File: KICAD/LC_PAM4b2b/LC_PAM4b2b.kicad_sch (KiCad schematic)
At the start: 18 parts, among them J1 Conn_01x02_Male, J10 Micro_SD_Board, J2 Conn_01x02_Male, J3 Conn_01x03_Pin, J4 Conn_01x02_Pin, J6 RTC, J7 Conn_01x03_Pin

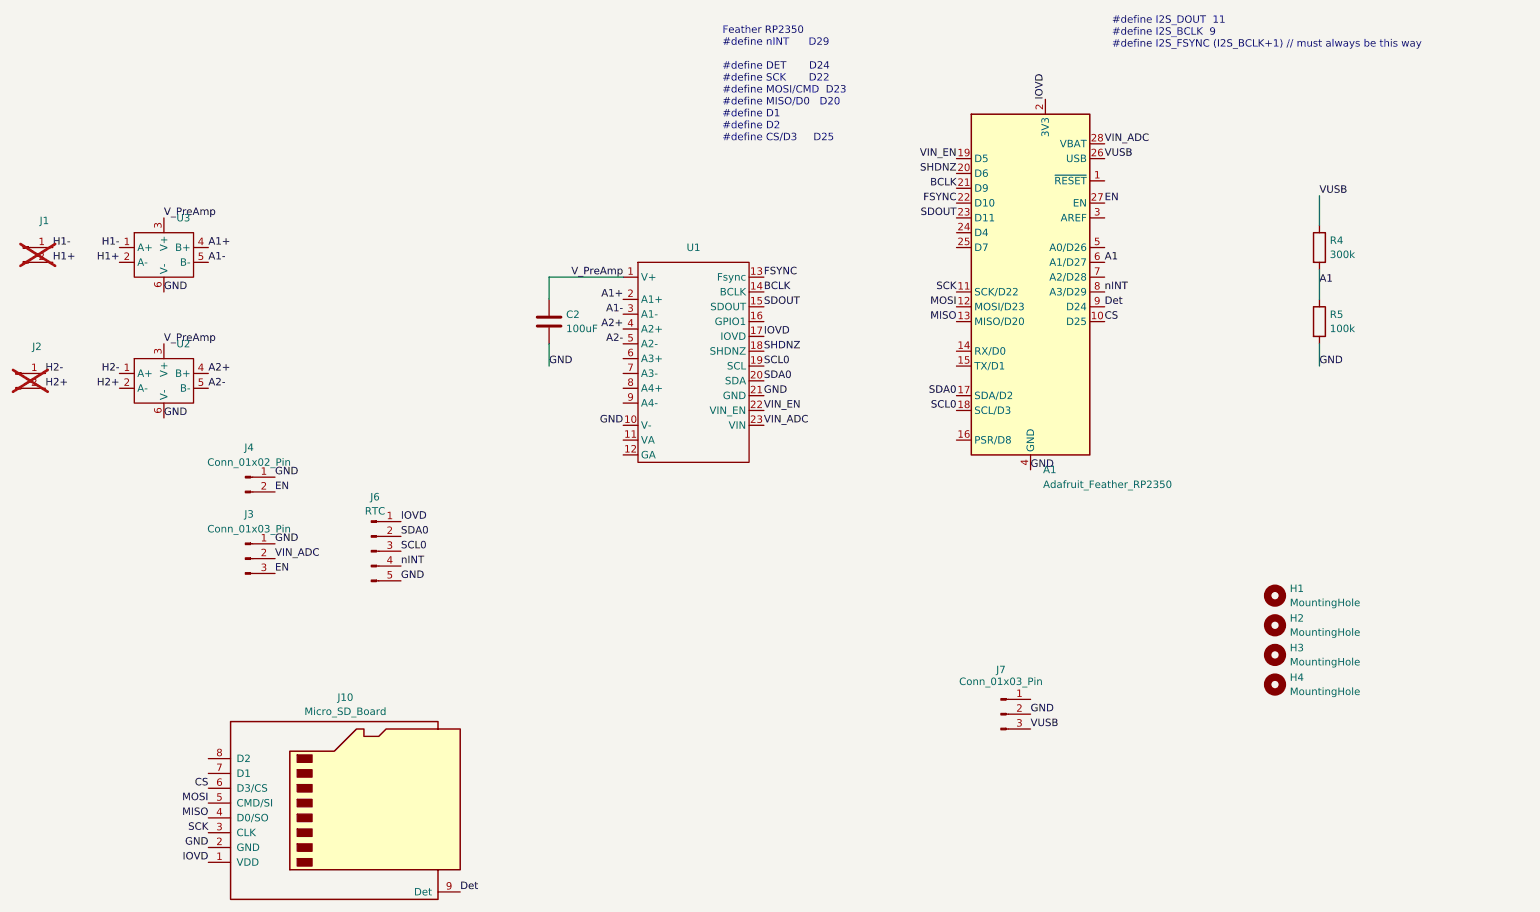
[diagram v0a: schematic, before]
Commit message: corrected hibernate
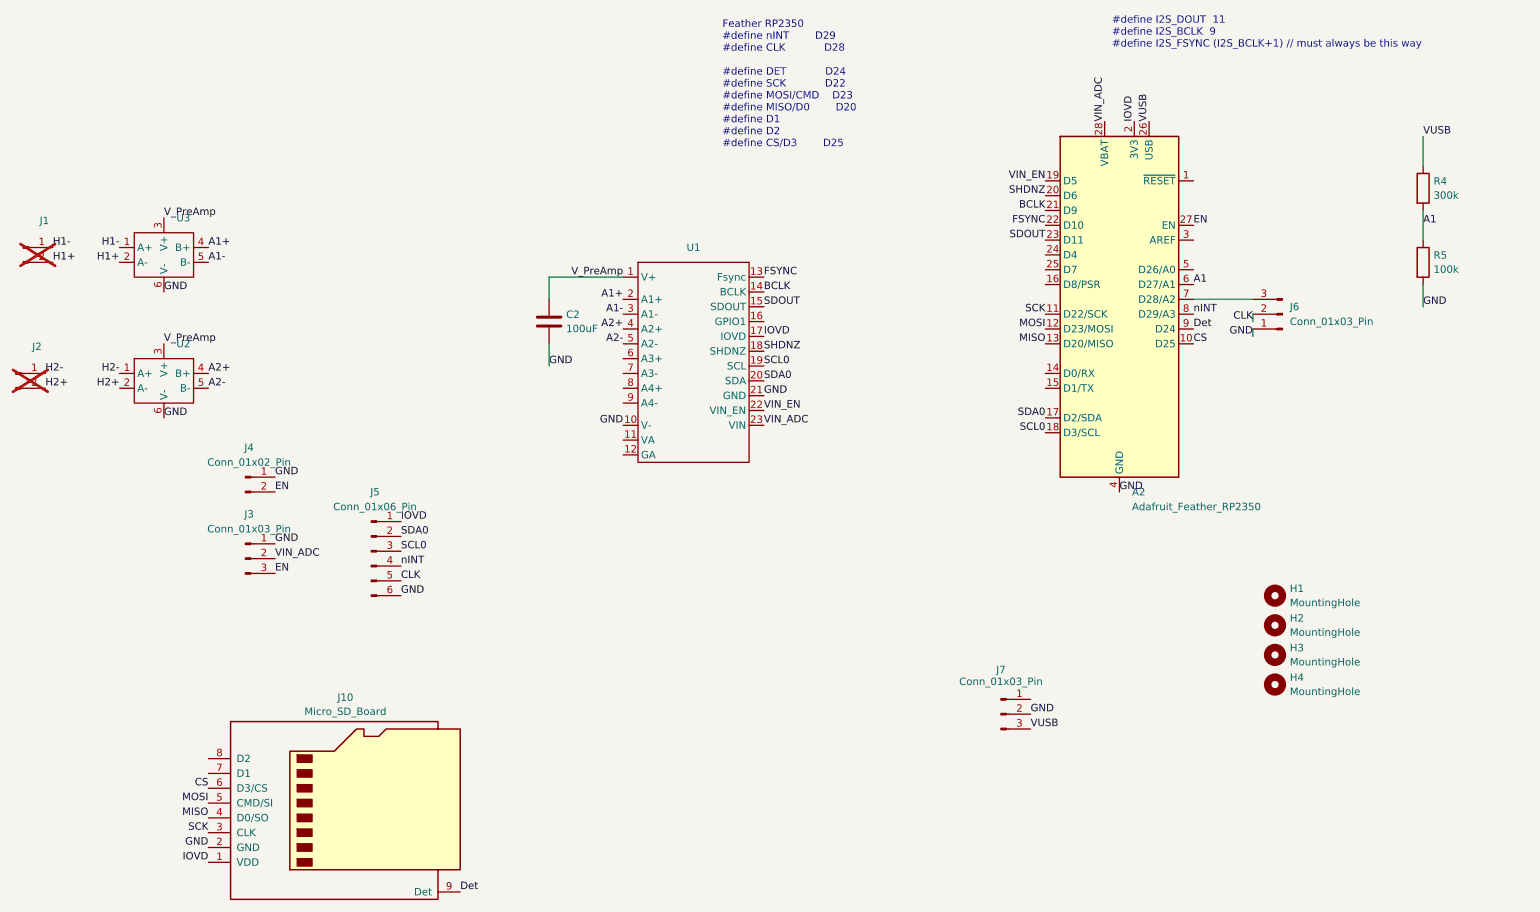
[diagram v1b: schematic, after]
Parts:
- removed A1: Adafruit_Feather_RP2350, Module:Adafruit_Feather_WithMountingHoles, symbol MCU_Module:Adafruit_Feather_M0_Adalogger
- removed J6: RTC, Connector_PinHeader_2.54mm:PinHeader_1x05_P2.54mm_Vertical, symbol Connector:Conn_01x05_Pin
- added A2: Adafruit_Feather_RP2350, Module:Adafruit_Feather, symbol myLIbrary:Adafruit_Feather_RP2350
- added J5: Conn_01x06_Pin, Connector_PinHeader_2.54mm:PinHeader_1x06_P2.54mm_Vertical, symbol Connector:Conn_01x06_Pin
- added J6: Conn_01x03_Pin, Connector_PinHeader_1.27mm:PinHeader_1x03_P1.27mm_Vertical, symbol Connector:Conn_01x03_Pin
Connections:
- net A1: now also A2.6 (D27/A1)
- net BCLK: now also A2.21 (D9)
- net CS: now also A2.10 (D25)
- net Det: now also A2.9 (D24)
- net EN: now also A2.27 (EN)
- net FSYNC: now also A2.22 (D10)
- net GND: now also A2.4 (GND), J5.6 (Pin_6), J6.1 (Pin_1)
- net IOVD: now also A2.2 (3V3), J5.1 (Pin_1)
- net MISO: now also A2.13 (D20/MISO)
- net MOSI: now also A2.12 (D23/MOSI)
- net SCK: now also A2.11 (D22/SCK)
- net SCL0: now also A2.18 (D3/SCL), J5.3 (Pin_3)
- net SDA0: now also A2.17 (D2/SDA), J5.2 (Pin_2)
- net SDOUT: now also A2.23 (D11)
- net SHDNZ: now also A2.20 (D6)
- net VIN_ADC: now also A2.28 (VBAT)
- net VIN_EN: now also A2.19 (D5)
- net VUSB: now also A2.26 (USB)
- net nINT: now also A2.8 (D29/A3), J5.4 (Pin_4)
- new net: A2.7 (D28/A2), J6.3 (Pin_3)
- new net CLK: J5.5 (Pin_5), J6.2 (Pin_2)
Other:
- note added: "Feather RP2350 #define nINT D29 #define CLK D28 #define DET D24 #define SCK D22 #define MOSI/CMD D23 #define MISO/D0 D20 #define D1 #define D2 #define CS/D3 D25"
- note removed: "Feather RP2350 #define nINT D29 #define DET D24 #define SCK D22 #define MOSI/CMD D23 #define MISO/D0 D20 #define D1 #define D2 #define CS/D3 D25"
- moved on the sheet: R4, R5
